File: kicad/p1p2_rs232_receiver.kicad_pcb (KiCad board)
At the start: 2 copper layers, 65 x 56.5 mm, 59 parts, among them J1 Raspberry_Pi_2_3, J2 PC MC_1,5_2-G-3.81, U1 LTV-817S, U103 LM4861, U2 LM317L_TO92, U3 Pico

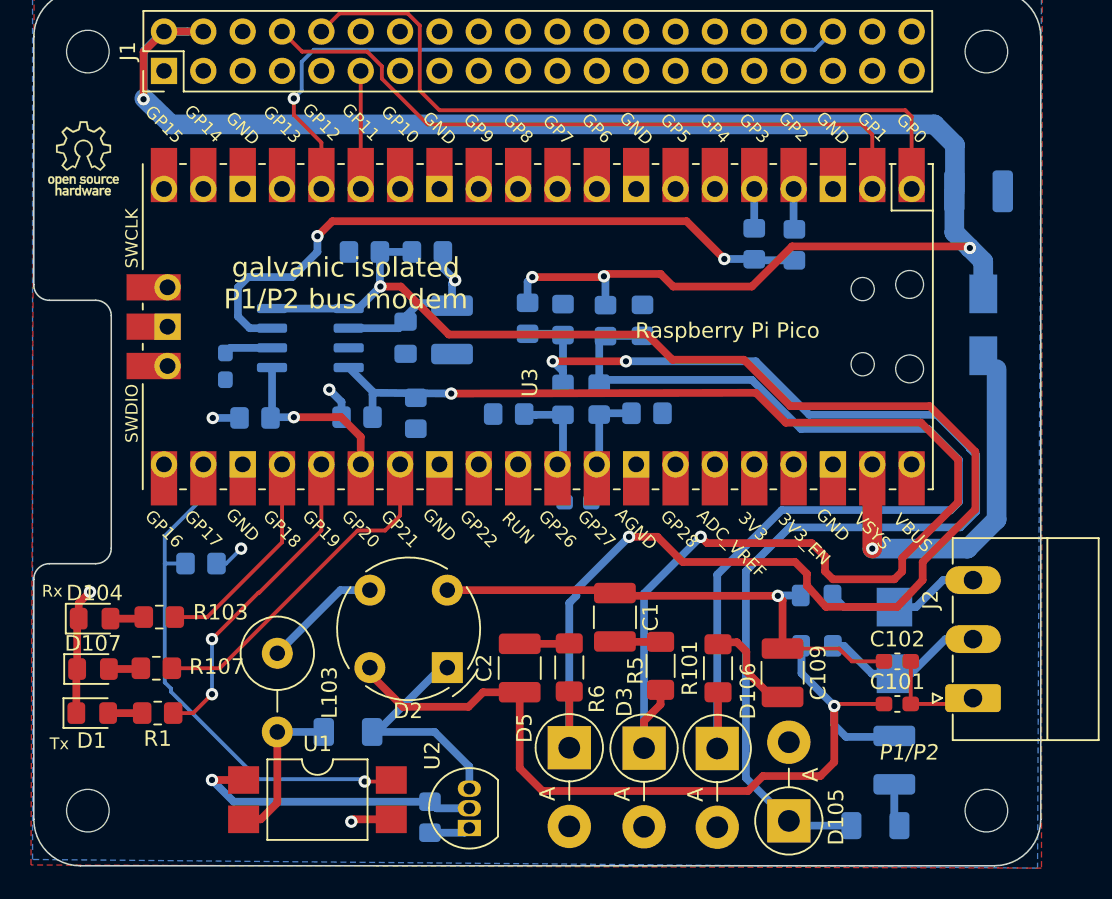
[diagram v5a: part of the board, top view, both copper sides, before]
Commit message: kicad: Update schematics
- Add common mode choke
- Use gain 5 for OpAmp
  The OpAmp is not stable at unity gain.
  The OpAmp is not stable with high impedance load (unconnected P1/P2 bus).
- Use OpAmp in inverting operation mode instead voltage follower mode
- Add 'DNP' pull down and capacitor on OpAmp feedback
  TODO: Figure out if required for stability.
- Replace DC bus level detection
- Use external precision 3.0V voltage shunt as ADC voltage
- Use 3.0V as bias voltage to reduce noise
- Add Pico reset button

Signed-off-by: Patrick Rudolph <rudolphpatrick05@gmail.com>
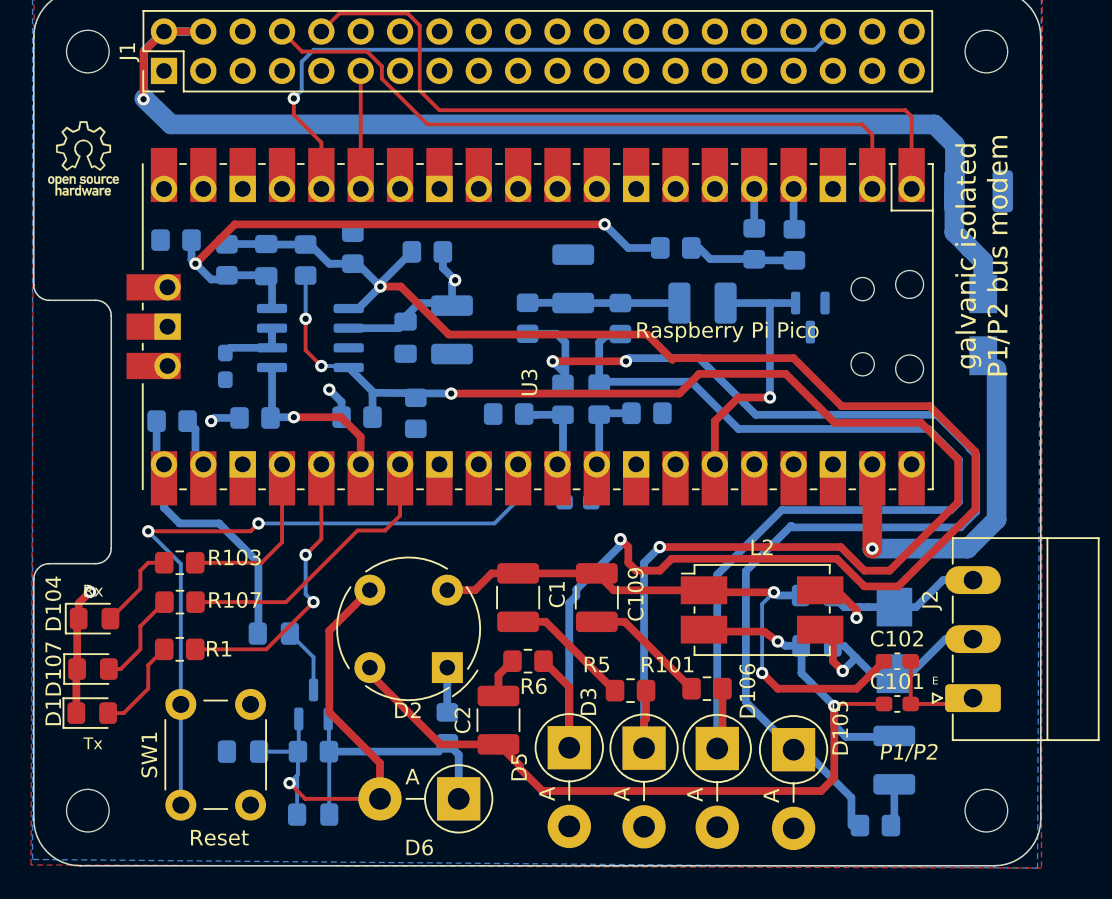
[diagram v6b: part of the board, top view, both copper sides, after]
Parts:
- removed L103: L-XHBCC 100M, Inductor_THT:L_Axial_L14.0mm_D4.5mm_P5.08mm_Vertical_Fastron_LACC
- removed R112, R117: 14k, Resistor_SMD:R_0805_2012Metric_Pad1.20x1.40mm_HandSolder
- removed U2: LM317L_TO92, Package_TO_SOT_THT:TO-92_Inline
- added C4: 10p, Capacitor_SMD:C_0805_2012Metric_Pad1.18x1.45mm_HandSolder, B.Cu at (70.1, 49.0)
- added C5: 100n, Capacitor_SMD:C_0805_2012Metric_Pad1.18x1.45mm_HandSolder, B.Cu at (70.6, 73.2)
- added C6: 100n, Capacitor_SMD:C_0805_2012Metric_Pad1.18x1.45mm_HandSolder, B.Cu at (68.6, 80.8)
- added C7: 1u, Capacitor_SMD:C_1210_3225Metric_Pad1.33x2.70mm_HandSolder, B.Cu at (89.9, 50.3)
- added D6: ZF 15, Diode_THT:D_5W_P5.08mm_Vertical_AnodeUp, F.Cu at (82.5, 83.8)
- added L1: 680u, Inductor_SMD:L_1210_3225Metric_Pad1.42x2.65mm_HandSolder, B.Cu at (98.3, 51.8)
- added L2: L_Coupled_1243, B82790C0:L_CommonMode_TDK_B82790C0, F.Cu at (102.1, 71.6)
- added Q1: BSS123, Package_TO_SOT_SMD:SOT-23, B.Cu at (73.2, 77.7)
- added R13: 2k2, Resistor_SMD:R_0805_2012Metric_Pad1.20x1.40mm_HandSolder, B.Cu at (64.0, 59.4)
- added R14: 47k, Resistor_SMD:R_0805_2012Metric_Pad1.20x1.40mm_HandSolder, B.Cu at (67.6, 49.0)
- added R15: 10k, Resistor_SMD:R_0805_2012Metric_Pad1.20x1.40mm_HandSolder, B.Cu at (73.1, 80.8)
- added R16: 10k, Resistor_SMD:R_0805_2012Metric_Pad1.20x1.40mm_HandSolder, B.Cu at (81.8, 79.2)
- added R17: 12k, Resistor_SMD:R_0805_2012Metric_Pad1.20x1.40mm_HandSolder, B.Cu at (72.6, 49.0)
- added SW1: SW_Push, Button_Switch_THT:SW_PUSH_6mm_H5mm, F.Cu at (64.6, 84.2)
- C107: value 1u -> 100n; footprint Capacitor_SMD:C_1206_3216Metric_Pad1.33x1.80mm_HandSolder -> Capacitor_SMD:C_0805_2012Metric_Pad1.18x1.45mm_HandSolder
- C113: value 100p -> 1u
- C115: value 220p -> 100p
- R10, R11, R12, R9: value 22k -> 10k
- R101, R102, R5, R6: footprint Resistor_SMD:R_1206_3216Metric_Pad1.30x1.75mm_HandSolder -> Resistor_SMD:R_0805_2012Metric_Pad1.20x1.40mm_HandSolder
- R109, R114: value 14k -> 6k2
- R110, R116: value 6k8 -> 12k
- R2: value 47k -> 10k
- R3: value 4k7 -> 10k
- R4: value 240 -> DNP
- R7, R8: value 12k2 -> 18k
- U1: value LTV-817S -> LM4040DBZ-3; footprint Package_DIP:SMDIP-4_W9.53mm -> Package_TO_SOT_SMD:SOT-23; moved to B.Cu
- moved U1 44.5 mm to (105.2, 52.8), turned to -90 degrees
- moved R4 40.7 mm to (64.3, 47.8), turned to 180 degrees
- moved R3 36.8 mm to (96.5, 48.3)
- moved C109 12.9 mm to (91.4, 70.8)
- moved C1 6.38 mm to (86.4, 70.8)
- moved C107 5.79 mm to (73.1, 84.8)
- moved D105 4.61 mm to (104.1, 80.6), turned to -90 degrees
- moved R107 4.53 mm to (64.5, 71.1)
- moved R1 4.35 mm to (64.5, 74.2)
- moved R103 3.75 mm to (64.5, 68.6)
- moved C2 3.63 mm to (85.1, 78.7)
- moved R6 2.70 mm to (87.0, 74.9), turned to 180 degrees
- moved R5 2.51 mm to (93.6, 76.8), turned to 180 degrees
- moved R101 1.50 mm to (98.6, 76.7), turned to 180 degrees
- moved R109 0.97 mm to (93.0, 52.8)
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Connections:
- net Net-(D4-Pad1) renamed +VDC
- D2 pad 1: Net-(C107-Pad1) -> Net-(D2-Pad1)
- D2 pad 3: Net-(D2-Pad3) -> Net-(C107-Pad2)
- D5 pad 1: Net-(D5-Pad1) -> Net-(C4-Pad2)
- R10 pad 1: Net-(D5-Pad1) -> Net-(C4-Pad2)
- R109 pad 1: +5V -> Net-(C7-Pad1)
- R114 pad 1: +5V -> Net-(C7-Pad1)
- R3 pad 1: +3V3 -> Net-(R104-Pad2)
- R3 pad 2: /CARRIER -> Net-(C4-Pad1)
- R4 pad 1: Net-(R4-Pad1) -> Net-(C4-Pad1)
- R4 pad 2: Net-(R4-Pad2) -> GND
- R6 pad 1: Net-(D5-Pad1) -> Net-(C4-Pad2)
- R9 pad 2: Net-(D5-Pad1) -> Net-(C4-Pad2)
- U1 pad 1: Net-(R4-Pad2) -> +3.3VADC
- U1 pad 2: Net-(C107-Pad2) -> GND
- U1 pad 3: GND -> (no net)
- U103 pad 3: Net-(R104-Pad2) -> Net-(C113-Pad1)
- U103 pad 4: Net-(D5-Pad1) -> Net-(C4-Pad1)
- U103 pad 5: Net-(D5-Pad1) -> Net-(C4-Pad2)
- U3 pad 21: unconnected-(U3-Pad21) -> /CARRIER_DETECT
- U3 pad 30: unconnected-(U3-Pad30) -> Net-(SW1-Pad1)
- U3 pad 35: +3V3 -> +3.3VADC
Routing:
- net Net-(C4-Pad2): track 0.00 -> 111.9 mm, vias 0 -> 2
- net Net-(D5-Pad1): track 105.3 -> 0.00 mm, vias 2 -> 0
- net Net-(SW1-Pad1): track 0.00 -> 45.6 mm, vias 0 -> 2
- net Net-(C4-Pad1): track 0.00 -> 40.7 mm, vias 0 -> 2
- net Net-(R104-Pad2): track 43.7 -> 6.98 mm, vias 2 -> 0
- net +5V: track 113.4 -> 79.9 mm, vias 4 -> 1
- net /CARRIER: track 33.9 -> 3.21 mm, vias 1 -> 0
- net Net-(C107-Pad2): track 10.2 -> 32.4 mm, vias 0 -> 1
- net Net-(R4-Pad2): track 19.4 -> 0.00 mm, vias 1 -> 0
- net /CARRIER_DETECT: track 0.00 -> 17.9 mm
- net +3.3VADC: track 0.00 -> 17.6 mm, vias 0 -> 1
- net Net-(C7-Pad1): track 0.00 -> 9.81 mm
- net Net-(D3-Pad1): track 86.4 -> 94.1 mm, vias 2 -> 4
- net Net-(D2-Pad3): track 7.27 -> 0.00 mm
- net Net-(C1-Pad2): track 2.96 -> 8.10 mm
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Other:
- board text added: "E"
- board text added: "Reset"

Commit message: kicad: Update schematic
Signed-off-by: Patrick Rudolph <rudolphpatrick05@gmail.com>
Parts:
- C4: value 10p -> 4p7
- D105, D106, D3, D5, D6: footprint Diode_THT:D_5W_P5.08mm_Vertical_AnodeUp -> Diode_THT:D_DO-41_SOD81_P5.08mm_Vertical_AnodeUp
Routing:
- net Net-(D105-Pad1): track 76.2 -> 76.8 mm

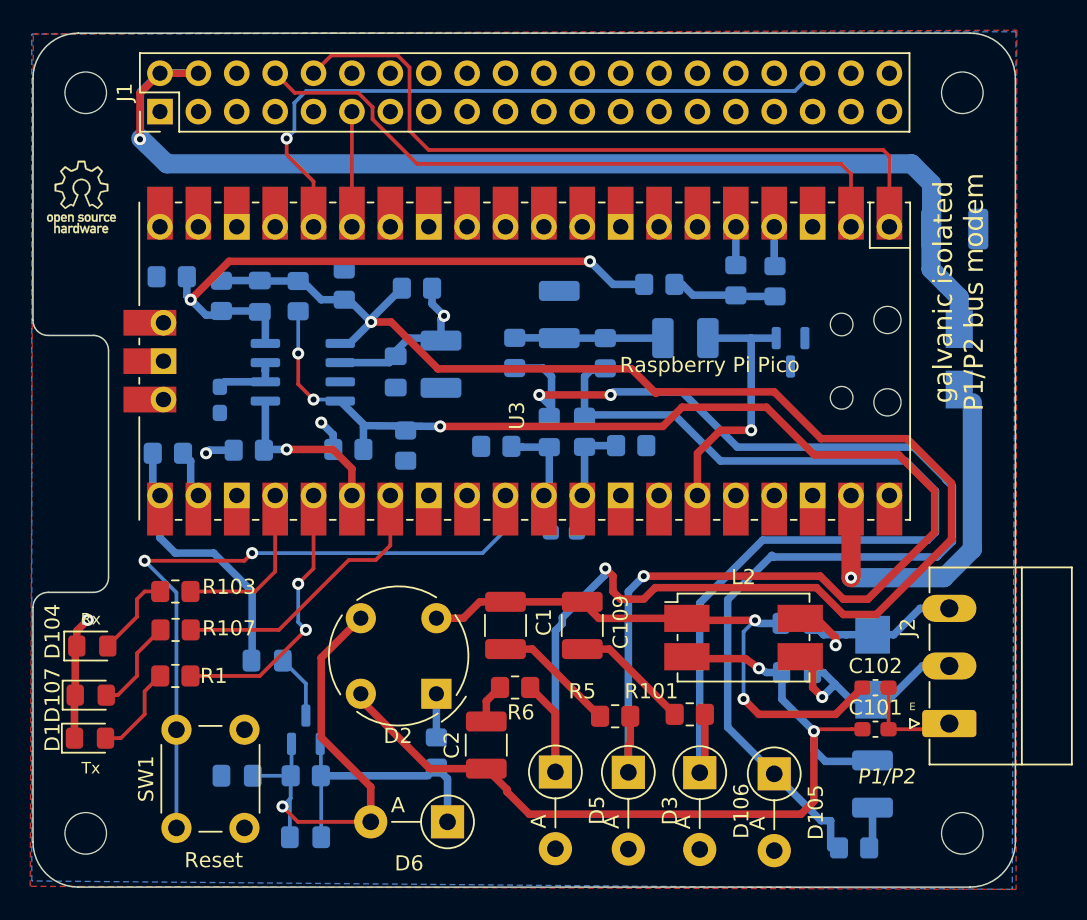
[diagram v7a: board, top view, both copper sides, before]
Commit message: kicad: Redesign to TX with more power
- Use 5V as LM4871 power supply
- Decrease output impedance to 4.5 Ohms
- Decrease input impedance to 1k Ohm
- AC couple input signal

Signed-off-by: Patrick Rudolph <rudolphpatrick05@gmail.com>
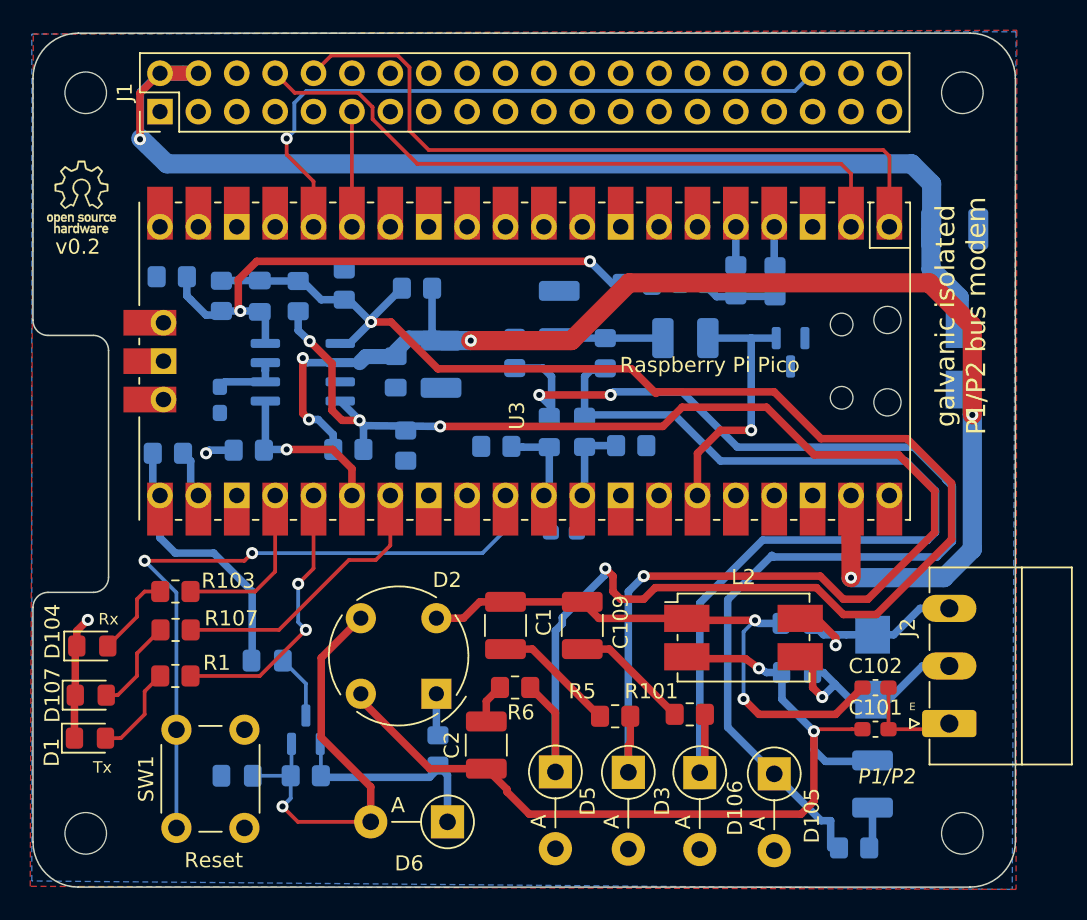
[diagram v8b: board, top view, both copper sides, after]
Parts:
- removed C107: 100n, Capacitor_SMD:C_0805_2012Metric_Pad1.18x1.45mm_HandSolder
- added C8: 100n, Capacitor_SMD:C_0603_1608Metric_Pad1.08x0.95mm_HandSolder, B.Cu at (98.8, 48.4)
- C1, C2: value 4u7 -> 6u8
- C4: value 4p7 -> 220p
- D3, D5: value ZF 3,6 -> ZF 5,6
- R104, R108: value 2k2 -> 1k
- R15: value 10k -> 100k
- R16: value 10k -> 220k
- R5, R6: value 2,2 -> 1
- U103: value LM4861 -> LM4871
- moved R3 1.49 mm to (95.0, 48.3)
- moved R16 0.17 mm to (81.9, 79.1)
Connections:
- C111 pad 2: +3V3 -> +VDC
- C112 pad 2: +3V3 -> +VDC
- R104 pad 2: Net-(R104-Pad2) -> Net-(C8-Pad1)
- R108 pad 1: Net-(R104-Pad2) -> Net-(C8-Pad1)
- R11 pad 1: +3V3 -> +VDC
- R3 pad 1: Net-(R104-Pad2) -> Net-(C8-Pad2)
- R9 pad 1: +3V3 -> +VDC
- U103 pad 6: +3V3 -> +VDC
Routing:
- net +VDC: track 25.2 -> 90.1 mm, vias 1 -> 5
- net +3V3: track 15.5 -> 1.91 mm, vias 3 -> 1
- net Net-(R104-Pad2): track 6.98 -> 0.00 mm
- net Net-(C8-Pad1): track 0.00 -> 4.83 mm
- net Net-(D6-Pad1): track 18.0 -> 14.4 mm
- net Net-(C4-Pad1): track 40.7 -> 37.9 mm
- net Net-(C6-Pad2): track 32.4 -> 29.9 mm
- net Net-(C8-Pad2): track 0.00 -> 1.89 mm
- net Net-(D3-Pad1): track 94.1 -> 95.8 mm
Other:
- board text added: "v0.2"
